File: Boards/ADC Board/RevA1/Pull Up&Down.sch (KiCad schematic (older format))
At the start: 4 parts, among them J3 Screw Terminals, J4 Jumper Terminals

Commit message: Added 12-pin and 4-pin spring terminal footprints. Updated footprints for ADC board. Continued work on PCB layout of ADC board.
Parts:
- J3: footprint Connector_PinHeader_2.54mm:PinHeader_1x03_P2.54mm_Vertical -> footprints:1985292
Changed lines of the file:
@@
 F 0 "J3" H 2500 950 50  0000 C CNN
 F 1 "Screw Terminals" H 2550 1050 50  0000 C CNN
-F 2 "Connector_PinHeader_2.54mm:PinHeader_1x03_P2.54mm_Vertical" H 2150 1200 50  0001 C CNN
+F 2 "footprints:1985292" H 2150 1200 50  0001 C CNN
 F 3 "~" H 2150 1200 50  0001 C CNN
 	1    2150 1200

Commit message: Imported 4 pin spring terminals. Replaced 12 pin terminals with 4 pin terminals on ADC board. Placed 4 pin terminals on PCB.
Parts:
- J3: footprint footprints:1985292 -> Spring_Terminal_4Pin:1984989
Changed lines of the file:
@@
 F 0 "J3" H 2500 950 50  0000 C CNN
 F 1 "Screw Terminals" H 2550 1050 50  0000 C CNN
-F 2 "footprints:1985292" H 2150 1200 50  0001 C CNN
+F 2 "Spring_Terminal_4Pin:1984989" H 2150 1200 50  0001 C CNN
 F 3 "~" H 2150 1200 50  0001 C CNN
 	1    2150 1200

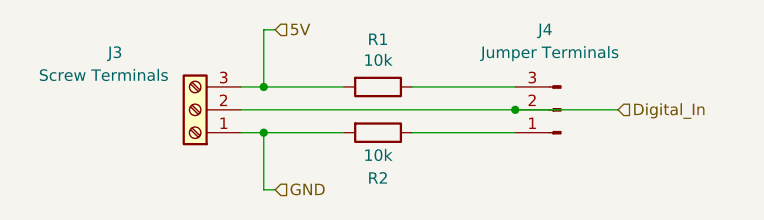
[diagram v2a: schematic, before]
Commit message: In process of updating ADC board to remove 5V connection from PI. Also commiting small changes to uV board.
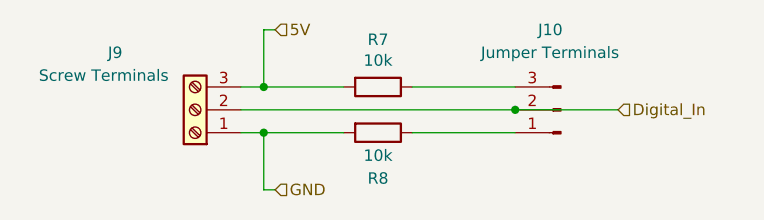
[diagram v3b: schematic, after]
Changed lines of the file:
@@
 AR Path="/616423D2/615FC6ED" Ref="J7"  Part="1"
 AR Path="/616425FE/615FC6ED" Ref="J9"  Part="1"
-F 0 "J3" H 2500 950 50  0000 C CNN
+F 0 "J9" H 2500 950 50  0000 C CNN
 F 1 "Screw Terminals" H 2550 1050 50  0000 C CNN
 F 2 "Spring_Terminal_4Pin:1984989" H 2150 1200 50  0001 C CNN
@@
 AR Path="/616423D2/616034B0" Ref="R5"  Part="1"
 AR Path="/616425FE/616034B0" Ref="R7"  Part="1"
-F 0 "R1" V 2743 1100 50  0000 C CNN
+F 0 "R7" V 2743 1100 50  0000 C CNN
 F 1 "10k" V 2834 1100 50  0000 C CNN
 F 2 "Resistor_SMD:R_0603_1608Metric" V 2880 1100 50  0001 C CNN
@@
 AR Path="/616423D2/61604CD1" Ref="R6"  Part="1"
 AR Path="/616425FE/61604CD1" Ref="R8"  Part="1"
-F 0 "R2" V 3150 1300 50  0000 C CNN
+F 0 "R8" V 3150 1300 50  0000 C CNN
 F 1 "10k" V 3050 1300 50  0000 C CNN
 F 2 "Resistor_SMD:R_0603_1608Metric" V 2880 1300 50  0001 C CNN
@@
 AR Path="/616423D2/61613676" Ref="J8"  Part="1"
 AR Path="/616425FE/61613676" Ref="J10"  Part="1"
-F 0 "J4" H 3850 850 50  0000 R CNN
+F 0 "J10" H 3850 850 50  0000 R CNN
 F 1 "Jumper Terminals" H 4100 950 50  0000 R CNN
 F 2 "Connector_PinHeader_2.54mm:PinHeader_1x03_P2.54mm_Vertical" H 3750 1200 50  0001 C CNN
